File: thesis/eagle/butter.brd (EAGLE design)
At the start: 100 x 80 mm, 16 parts, among them U1 ADCS7477, U10 CD4051BPWR, U11 CD4051BPWR, U12 CD4051BPWR, U13 CD4051BPWR, U14 CD4051BPWR, U15 CD4051BPWR, U16 CD4051BPWR, U2 ADCS7477, U3 ADCS7477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

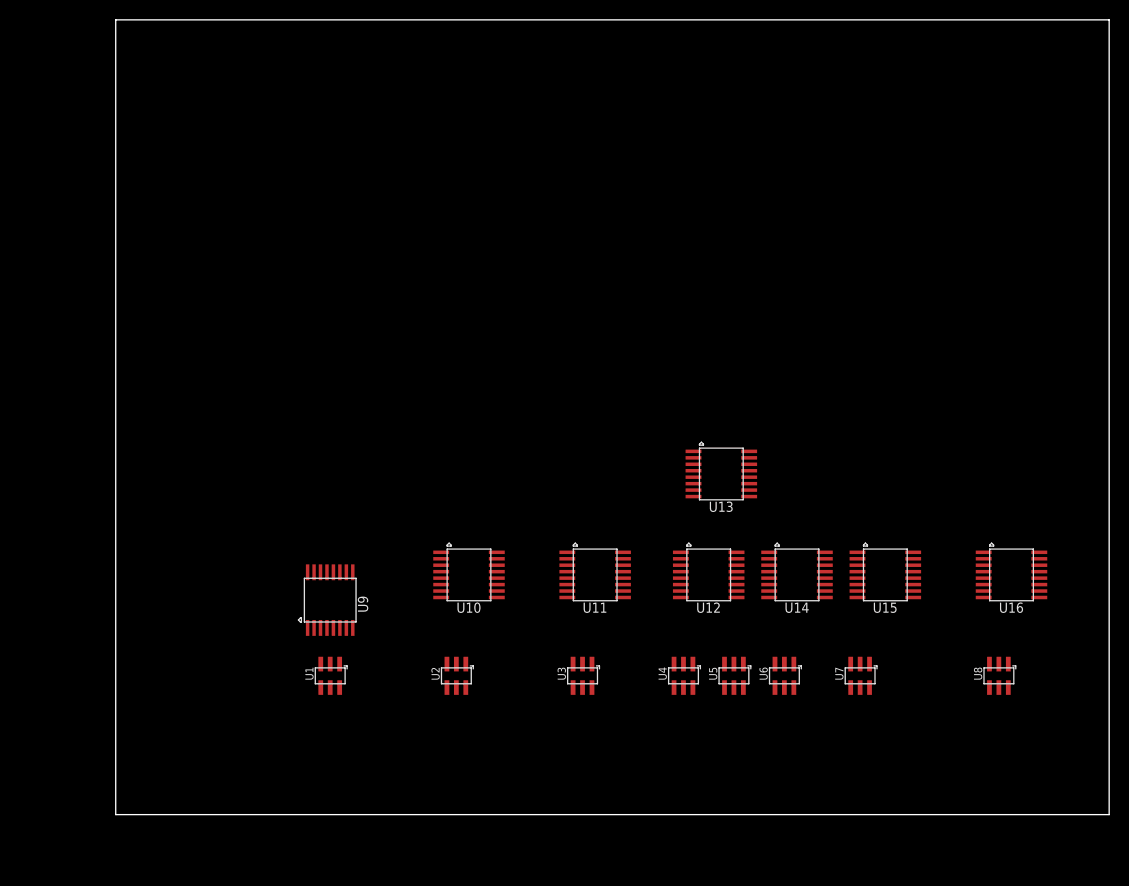
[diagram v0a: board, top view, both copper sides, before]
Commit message: added stm32f4 breakout to design, starting with two ADCs and two multiplexers
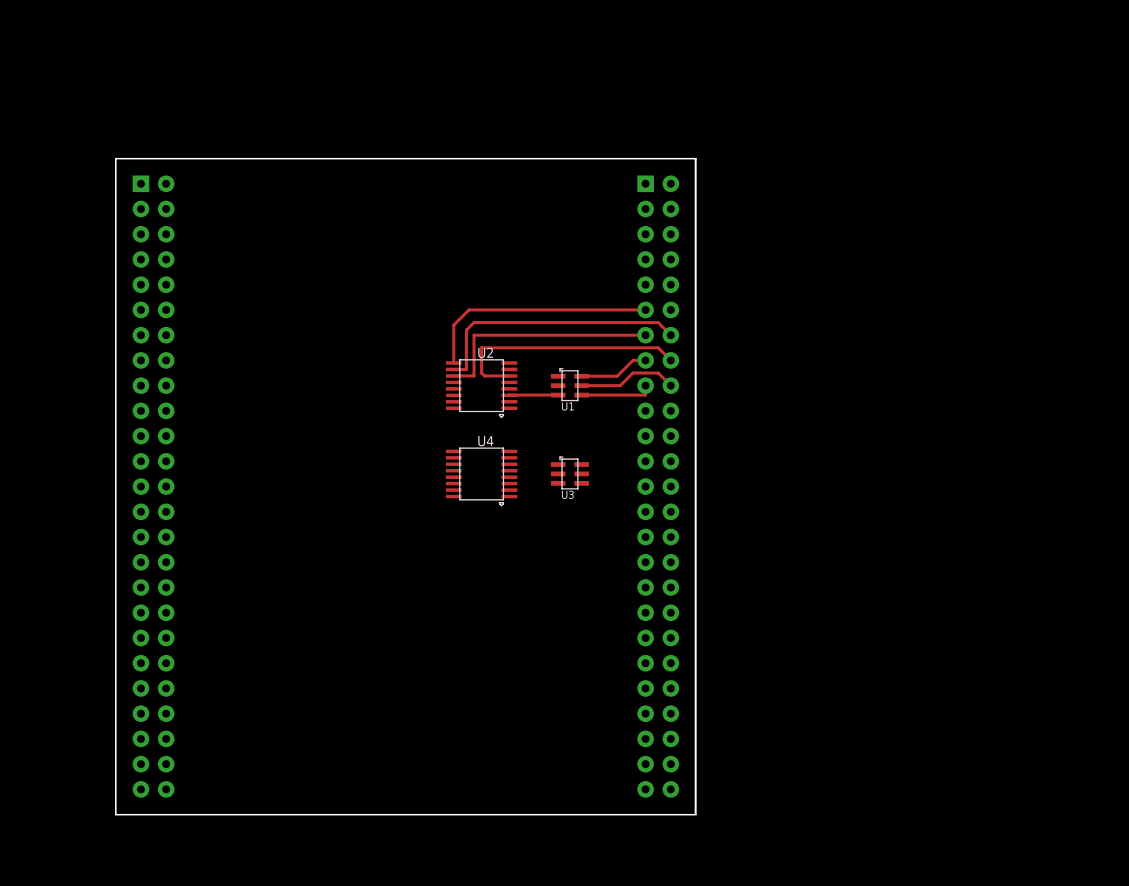
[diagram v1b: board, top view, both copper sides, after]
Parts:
- removed U10, U11, U12, U13, U14, U15, U16, U9: CD4051BPWR, butter:TSSOP-16
- removed U5, U6, U7, U8: ADCS7477, butter:SOT-23-6
- added U$1: STM32F4-DISCOVERY, STM32F4-DISCOVERY:STM32F4-DISCOVERY
- U2, U4: value ADCS7477 -> CD4051BPWR; device butter:SOT-23-6 -> butter:TSSOP-16
- moved U1 37.9 mm to (45.7, 43.2), turned to 0 degrees
- moved U2 29.3 mm to (36.8, 43.2), turned to 180 degrees
- moved U4 28.7 mm to (36.8, 34.3), turned to 180 degrees
- moved U3 20.4 mm to (45.7, 34.3), turned to 0 degrees
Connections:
- net !CS4 renamed !E2
- removed net !CS3: U3.P$6
- removed net !CS5: U5.P$6
- removed net !CS6: U6.P$6
- removed net !CS7: U7.P$6
- removed net !CS8: U8.P$6
- removed net D3: U3.P$5
- removed net D4: U4.P$5
- removed net D5: U5.P$5
- removed net D6: U6.P$5
- removed net D7: U7.P$5
- removed net D8: U8.P$5
- removed net N$3: U11.P$3, U3.P$3
- removed net N$4: U12.P$3, U4.P$3
- removed net N$5: U13.P$3, U5.P$3
- removed net N$6: U14.P$3, U6.P$3
- removed net N$7: U15.P$3, U7.P$3
- removed net N$8: U16.P$3, U8.P$3
- new net !E1: U$1.P$66, U2.P$6
- new net 1S0: U$1.P$63, U2.P$11
- new net 1S1: U$1.P$64, U2.P$10
- new net 1S2: U$1.P$61, U2.P$9
- new net 2S0: U4.P$11
- new net 2S1: U4.P$10
- new net 2S2: U4.P$9
- new net VEE: U2.P$7, U4.P$7
- net !CS1: now also U$1.P$65
- net !CS2: now also U3.P$6; no longer U2.P$6
- net D1: now also U$1.P$68
- net D2: now also U3.P$5; no longer U2.P$5
- net GND: now also U2.P$8, U4.P$8; no longer U2.P$2, U4.P$2, U5.P$2, U6.P$2, U7.P$2, U8.P$2
- net N$1: now also U2.P$3; no longer U9.P$3
- net N$2: now also U3.P$3, U4.P$3; no longer U10.P$3, U2.P$3
- net SCK: now also U$1.P$67; no longer U2.P$4, U4.P$4, U5.P$4, U6.P$4, U7.P$4, U8.P$4
- net VCC: now also U2.P$16, U4.P$16; no longer U2.P$1, U4.P$1, U5.P$1, U6.P$1, U7.P$1, U8.P$1
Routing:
- net 1S1: track 0.00 -> 26.7 mm
- net !E1: track 0.00 -> 25.0 mm
- net 1S2: track 0.00 -> 23.8 mm
- net 1S0: track 0.00 -> 23.4 mm
- net D1: track 0.00 -> 10.0 mm
- net SCK: track 0.00 -> 7.39 mm
- net !CS1: track 0.00 -> 7.10 mm
- net N$1: track 0.00 -> 4.93 mm
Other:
- board size 100 x 80 mm -> 58.3 x 66 mm

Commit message: started designing rail interface
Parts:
- added IC1: TL072D, linear:SO08
- added JP1: (no value), pinhead:1X01
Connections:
- new net V+: IC1.8
- new net V-: IC1.4
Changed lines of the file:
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@@
 <element name="U4" library="butter" package="TSSOP-16" value="CD4051BPWR" x="36.83" y="34.29" rot="R180"/>
 <element name="U$1" library="STM32F4-DISCOVERY" package="STM32F4-DISCOVERY" value="STM32F4-DISCOVERY" x="30.48" y="33.02"/>
+<element name="IC1" library="linear" package="SO08" value="TL072D" x="-5.08" y="3.81"/>
+<element name="JP1" library="pinhead" package="1X01" value="" x="-6.35" y="-3.81"/>
 </elements>
 <signals>
@@
 <wire x1="52.07" y1="45.72" x2="53.34" y2="45.72" width="0.3048" layer="1"/>
 </signal>
+<signal name="V+">
+<contactref element="IC1" pad="8"/>
+</signal>
+<signal name="V-">
+<contactref element="IC1" pad="4"/>
+</signal>
 </signals>

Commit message: whatever, fuck it
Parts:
- removed JP1: (no value), pinhead:1X01
- removed U3: ADCS7477, butter:SOT-23-6
- removed U4: CD4051BPWR, butter:TSSOP-16
- added R1, R2, R3: (no value), resistor:R0603
- added U$10, U$11, U$12, U$13, U$2, U$7, U$8, U$9: DG467, butter:TSSOP-6
- added U$3, U$4, U$5, U$6: RAILSEP, butter:RAIL
- moved IC1 59.4 mm to (39.4, 43.2), turned to 90 degrees
- moved U2 6.35 mm to (30.5, 43.2)
- moved U1 2.54 mm to (48.3, 43.2)
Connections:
- removed net !CS2: U3.P$6
- removed net !E2: U4.P$6
- removed net 2S0: U4.P$11
- removed net 2S1: U4.P$10
- removed net 2S2: U4.P$9
- removed net D2: U3.P$5
- removed net V+: IC1.8
- removed net V-: IC1.4
- new net N$10: U$11.P$6, U$5.P$2, U2.P$5
- new net N$11: U$12.P$6, U$6.P$1, U2.P$2
- new net N$12: U$13.P$6, U$6.P$2, U2.P$4
- new net N$13: U$2.P$3
- new net N$14: U$8.P$3
- new net N$15: U$10.P$3
- new net N$16: U$12.P$3
- new net N$17: U$7.P$3
- new net N$18: U$9.P$3
- new net N$19: U$11.P$3
- new net N$20: U$13.P$3
- new net N$21: U$10.P$1, U$11.P$1, U$12.P$1, U$13.P$1, U$2.P$1, U$7.P$1, U$8.P$1, U$9.P$1
- new net N$3: U$2.P$6, U$3.P$1, U2.P$13
- new net N$4: IC1.5, U2.P$3
- new net N$5: IC1.2, R1.1, R2.2, R3.2
- new net N$6: IC1.6, IC1.7, R1.2
- new net N$7: U$4.P$1, U$8.P$6, U2.P$15
- new net N$8: U$4.P$2, U$9.P$6, U2.P$12
- new net N$9: U$10.P$6, U$5.P$1, U2.P$1
- net GND: now also IC1.3, U$10.P$4, U$11.P$4, U$12.P$4, U$13.P$4, U$2.P$4, U$7.P$4, U$8.P$4, U$9.P$4; no longer U3.P$2, U4.P$8
- net N$1: now also IC1.1, R2.1; no longer U2.P$3
- net N$2: now also U$3.P$2, U$7.P$6, U2.P$14; no longer U3.P$3, U4.P$3
- net SCK: no longer U3.P$4
- net VCC: now also IC1.8, U$10.P$5, U$11.P$5, U$12.P$5, U$13.P$5, U$2.P$5, U$7.P$5, U$8.P$5, U$9.P$5; no longer U3.P$1, U4.P$16
- net VEE: now also IC1.4, U$10.P$2, U$11.P$2, U$12.P$2, U$13.P$2, U$2.P$2, U$7.P$2, U$8.P$2, U$9.P$2; no longer U4.P$7
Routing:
- net GND: track 0.00 -> 16.8 mm
- net VCC: track 0.00 -> 13.9 mm
- net N$5: track 0.00 -> 10.8 mm
- net N$4: track 0.00 -> 6.37 mm
- net 1S2: track 23.8 -> 30.1 mm
- net 1S1: track 26.7 -> 33.0 mm
- net 1S0: track 23.4 -> 29.8 mm
- net !E1: track 25.0 -> 31.4 mm
- net N$6: track 0.00 -> 6.20 mm
- net SCK: track 7.39 -> 4.85 mm
- net D1: track 10.0 -> 7.49 mm
- net !CS1: track 7.10 -> 4.56 mm
- net N$1: track 4.93 -> 6.06 mm

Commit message: rev 1a!
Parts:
- added C1, C3, C6: .1u, rcl:C0805
- added C2, C4, C7: 1u, rcl:C0805
- added C5: (no value), rcl:C0805
- added JMP1, JMP2, JMP3, JMP4: (no value), butter:JMP
- added JP1: (no value), pinhead:1X03
- added R4, R5, R6, R7: (no value), resistor:R0603
- added U3: (no value), butter:MSOP-10
- moved U$11 29.0 mm to (44.5, 63.5)
- moved U$2 29.0 mm to (16.5, 53.3)
- moved U$10 28.9 mm to (16.5, 63.2)
- moved U$7 28.2 mm to (44.5, 56.9), turned to 180 degrees
- moved U$13 23.9 mm to (44.5, 60.2)
- moved U$12 23.8 mm to (16.5, 59.9)
- moved U$9 23.4 mm to (44.5, 53.6), turned to 180 degrees
- moved U$8 22.9 mm to (16.5, 56.6)
- moved U2 16.0 mm to (30.2, 59.2), turned to 0 degrees
- moved R3 10.6 mm to (47.2, 35.3), turned to 0 degrees
- moved IC1 8.41 mm to (35.3, 35.8)
- moved U$5 6.35 mm to (30.5, 62.2), turned to 180 degrees
- moved U$6 6.35 mm to (30.5, 59.7), turned to 180 degrees
- moved R2 5.86 mm to (38.6, 41.4)
- moved R1 4.52 mm to (35.8, 42.2)
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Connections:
- new net !CSP1: U$1.P$69, U3.P$6
- new net +5V: C1.1, C2.1, C3.1, C4.1, C6.1, C7.1, R4.2, U$1.P$53, U1.P$1, U3.P$10
- new net N$22: IC1.3, JMP3.P$2, R1.1, R2.2, R7.1
- new net N$23: R3.2, R4.1, U3.P$4
- new net N$24: JMP2.P$2, JMP3.P$1, JMP4.P$1, U1.P$3
- new net N$25: U3.P$8
- new net N$26: IC1.1, JMP4.P$2, R5.1
- new net N$27: R7.2, U3.P$2
- net D1: now also U3.P$7
- net GND: now also C1.2, C2.2, C3.2, C4.2, C6.2, C7.2, JP1.2, R3.1, R6.1, U$1.P$99, U3.P$5; no longer IC1.3
- net N$1: now also IC1.2, R5.2, R6.2; no longer IC1.1, R2.1, U1.P$3
- net N$10: now also U$5.P$R, U2.P$15; no longer U$5.P$2, U2.P$5
- net N$11: now also U$6.P$L; no longer U$6.P$1
- net N$12: now also U$6.P$R, U2.P$14; no longer U$6.P$2, U2.P$4
- net N$2: now also U$3.P$R, U2.P$13; no longer U$3.P$2, U2.P$14
- net N$3: now also U$4.P$L, U2.P$5; no longer U$3.P$1, U2.P$13
- net N$4: now also JMP1.P$2
- net N$5: now also JMP2.P$1, U3.P$1; no longer IC1.2, R1.1, R2.2, R3.2
- net N$6: now also JMP1.P$1
- net N$7: now also U$3.P$L, U2.P$4; no longer U$4.P$1, U2.P$15
- net N$8: now also U$4.P$R; no longer U$4.P$2
- net N$9: now also U$5.P$L; no longer U$5.P$1
- net SCK: now also U3.P$9
- net VCC: now also JP1.3; no longer U1.P$1
- net VEE: now also JP1.1, R2.1
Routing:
- net 1S1: track 33.0 -> 0.00 mm
- net !E1: track 31.4 -> 0.00 mm
- net 1S2: track 30.1 -> 0.00 mm
- net 1S0: track 29.8 -> 0.00 mm
- net +5V: track 0.00 -> 20.6 mm
- net N$22: track 0.00 -> 15.3 mm
- net N$26: track 0.00 -> 14.8 mm
- net VCC: track 13.9 -> 0.00 mm
- net D1: track 7.49 -> 18.1 mm
- net !CSP1: track 0.00 -> 9.43 mm
- net N$5: track 10.8 -> 3.48 mm
- net N$23: track 0.00 -> 7.18 mm
- net N$6: track 6.20 -> 12.0 mm
- net GND: track 16.8 -> 11.2 mm
- net N$24: track 0.00 -> 5.48 mm
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
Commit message: not sure what's new here, but updated butter board
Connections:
- net +5V: now also C5.1
- net GND: now also C5.2
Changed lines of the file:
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@@
 <wire x1="43.18" y1="43.18" x2="43.18" y2="44.008" width="0.254" layer="1"/>
 <wire x1="45.212" y1="44.008" x2="45.212" y2="43.18" width="0.254" layer="1"/>
+<wire x1="47.056" y1="32.004" x2="46.394" y2="32.004" width="0.4064" layer="1"/>
+<wire x1="46.394" y1="32.004" x2="46.394" y2="35.306" width="0.4064" layer="1"/>
+<contactref element="C5" pad="2"/>
 <wire x1="43.28921875" y1="61.1378" x2="43.28921875" y2="64.4398" width="0" layer="19" extent="1-1"/>
 <wire x1="43.28921875" y1="57.8358" x2="43.28921875" y2="61.1378" width="0" layer="19" extent="1-1"/>
@@
 <wire x1="46.26" y1="36.846" x2="47.818" y2="40.386" width="0" layer="19" extent="1-1"/>
 <wire x1="40.132" y1="33.44" x2="46.26" y2="35.306" width="0" layer="19" extent="1-1"/>
-<wire x1="42.164" y1="26.162" x2="47.056" y2="32.004" width="0" layer="19" extent="1-1"/>
-<wire x1="27.426" y1="56.907" x2="43.28921875" y2="57.8358" width="0" layer="19" extent="1-1"/>
+<wire x1="42.164" y1="26.162" x2="46.394" y2="32.004" width="0" layer="19" extent="1-1"/>
+<wire x1="31.43" y1="50.292" x2="43.28921875" y2="54.5338" width="0" layer="19" extent="1-1"/>
+<wire x1="27.366" y1="49.022" x2="31.43" y2="50.292" width="0" layer="19" extent="1-1"/>
+<wire x1="27.426" y1="56.907" x2="31.43" y2="50.292" width="0" layer="19" extent="1-1"/>
 <wire x1="17.67078125" y1="55.7022" x2="27.426" y2="56.907" width="0" layer="19" extent="1-1"/>
 <wire x1="17.67078125" y1="59.0042" x2="17.67078125" y2="55.7022" width="0" layer="19" extent="1-1"/>
 <wire x1="17.67078125" y1="62.3062" x2="17.67078125" y2="59.0042" width="0" layer="19" extent="1-1"/>
 <wire x1="17.67078125" y1="52.4002" x2="17.67078125" y2="55.7022" width="0" layer="19" extent="1-1"/>
+<wire x1="26.35" y1="32.258" x2="40.132" y2="33.44" width="0" layer="19" extent="1-1"/>
 <wire x1="53.34" y1="2.54" x2="42.164" y2="26.162" width="0" layer="19" extent="1-1"/>
-<wire x1="31.43" y1="50.292" x2="53.34" y2="2.54" width="0" layer="19" extent="1-1"/>
-<wire x1="27.366" y1="49.022" x2="31.43" y2="50.292" width="0" layer="19" extent="1-1"/>
-<wire x1="47.056" y1="32.004" x2="46.394" y2="32.004" width="0.4064" layer="1"/>
-<wire x1="46.394" y1="32.004" x2="46.394" y2="35.306" width="0.4064" layer="1"/>
 </signal>
 <signal name="SCK">
@@
 <wire x1="51.308" y1="35.56" x2="49.784" y2="35.56" width="0.4064" layer="1"/>
 <wire x1="49.784" y1="35.56" x2="49.784" y2="35.394" width="0.4064" layer="1"/>
+<contactref element="C5" pad="1"/>
 <wire x1="47.0789" y1="45.908" x2="53.34" y2="60.96" width="0" layer="19" extent="1-1"/>
 <wire x1="45.212" y1="45.908" x2="47.0789" y2="45.908" width="0" layer="19" extent="1-1"/>
@@
 <wire x1="29.53" y1="50.292" x2="43.18" y2="45.908" width="0" layer="19" extent="1-1"/>
 <wire x1="25.466" y1="49.022" x2="29.53" y2="50.292" width="0" layer="19" extent="1-1"/>
+<wire x1="24.45" y1="32.258" x2="25.466" y2="49.022" width="0" layer="19" extent="1-1"/>
 </signal>
 <signal name="N$5">
